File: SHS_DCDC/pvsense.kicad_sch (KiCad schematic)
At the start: 15 parts, among them Q18 BSS84, Q19 2N7002, U3 LMV324AIDR

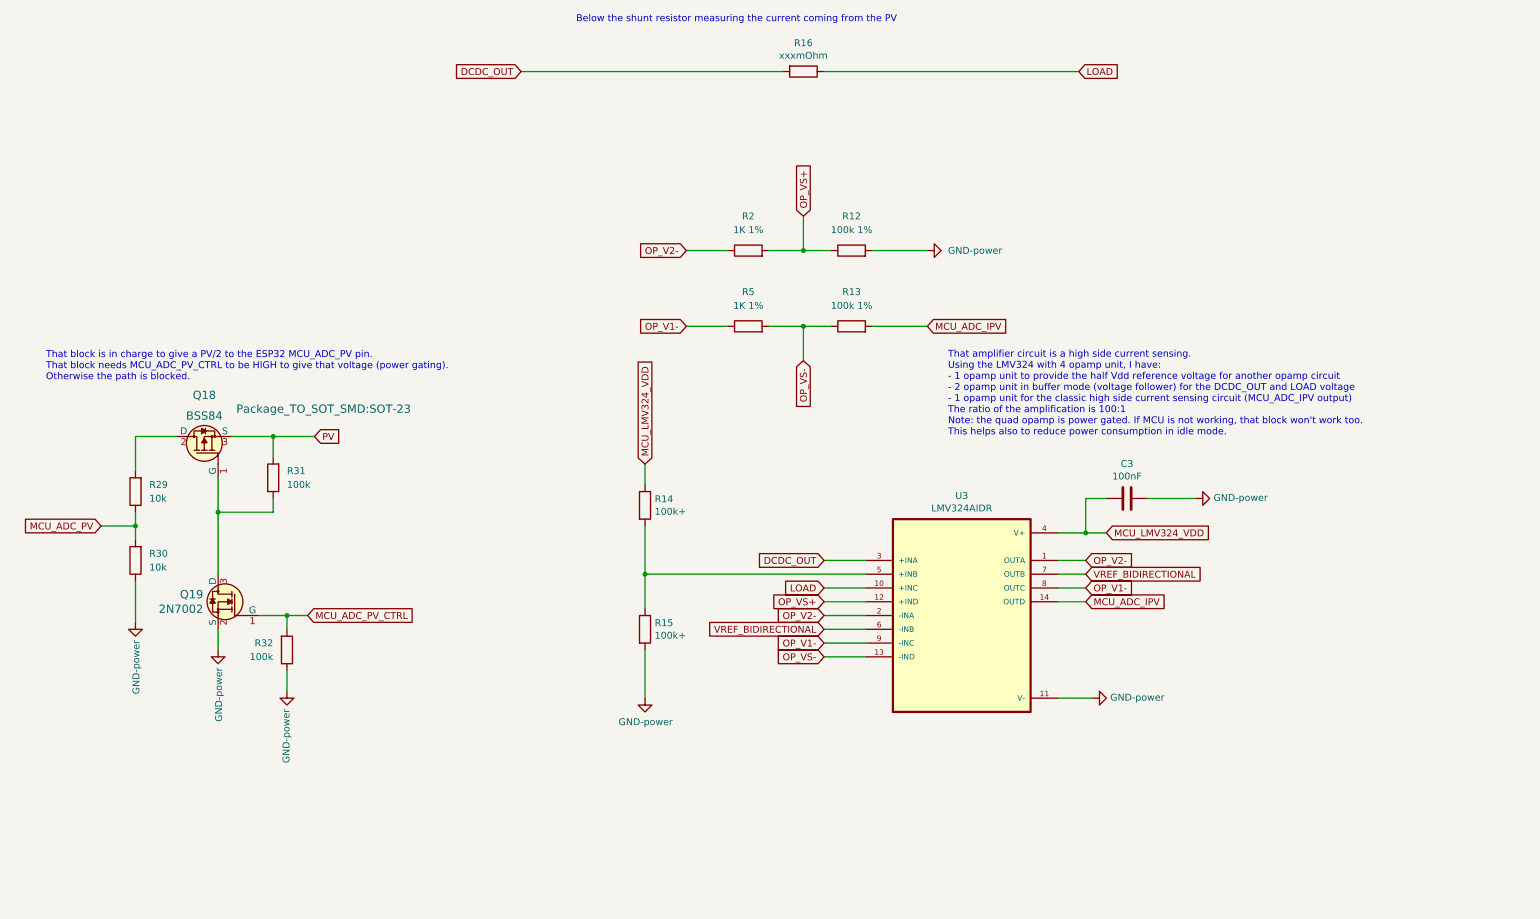
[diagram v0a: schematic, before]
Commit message: Commit before reannotation
Plan to test the reannotation feature.
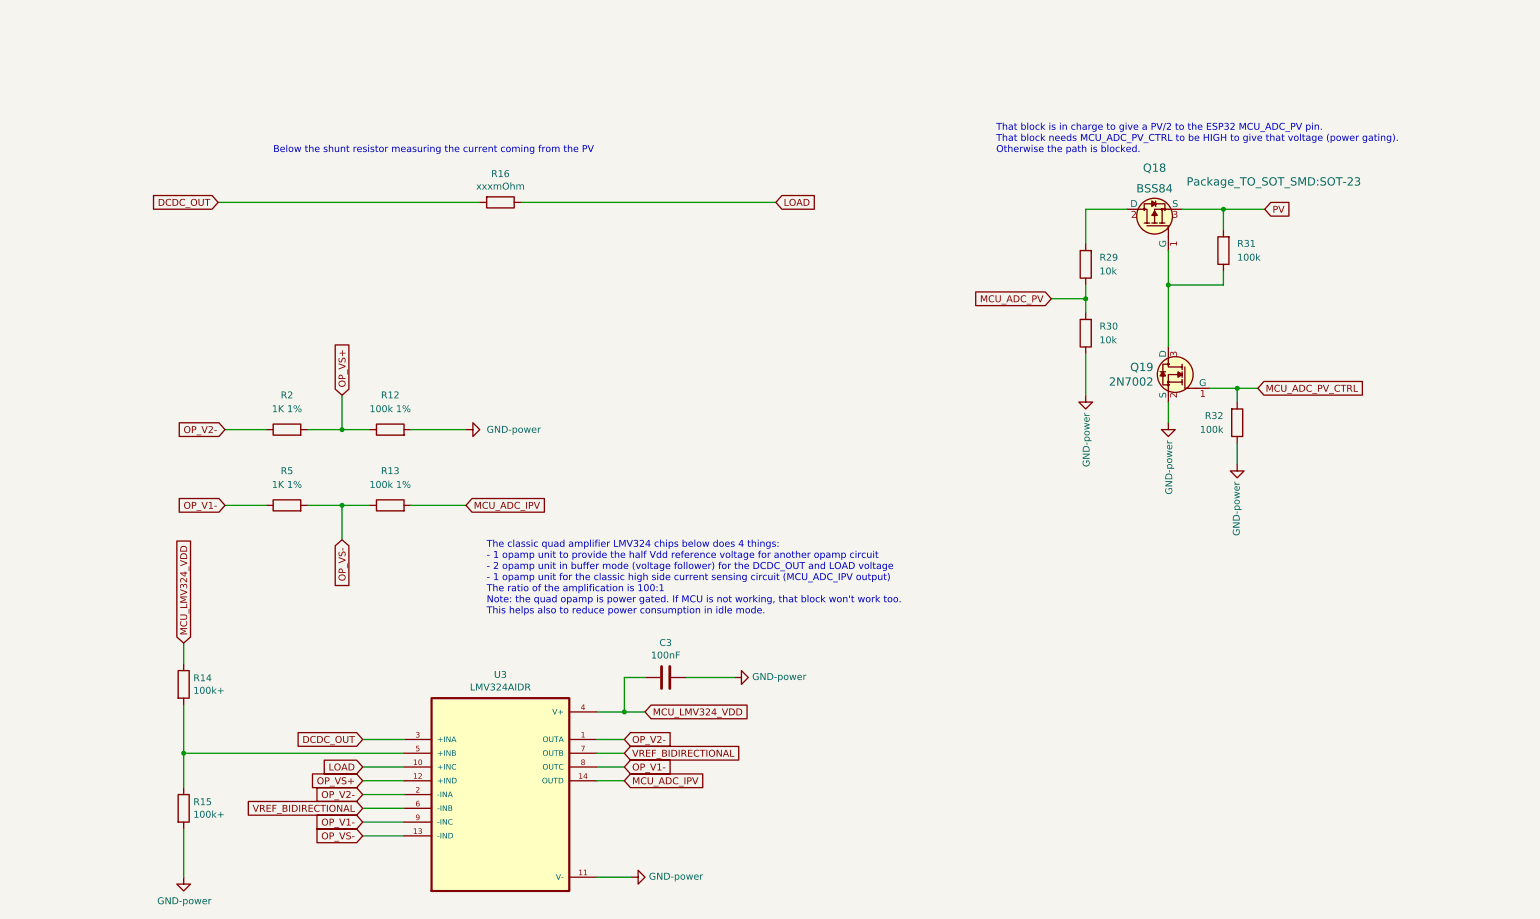
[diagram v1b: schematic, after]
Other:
- note added: "The classic quad amplifier LMV324 chips below does 4 things: - 1 opamp unit to provide the half Vdd reference voltage for another opamp circuit - 2 opamp unit in buffer mode (voltage follower) for the DCDC_OUT and LOAD voltage - 1 opamp unit for the classic high side current sensing circuit (MCU_ADC_IPV output) The ratio of the amplification is 100:1 Note: the quad opamp is power gated. If MCU is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"
- note removed: "That amplifier circuit is a high side current sensing. Using the LMV324 with 4 opamp unit, I have: - 1 opamp unit to provide the half Vdd reference voltage for another opamp circuit - 2 opamp unit in buffer mode (voltage follower) for the DCDC_OUT and LOAD voltage - 1 opamp unit for the classic high side current sensing circuit (MCU_ADC_IPV output) The ratio of the amplification is 100:1 Note: th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"
- moved on the sheet: C3, Q18, Q19, R12, R13, R14, R15, R16, R2, R29, R30, R31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

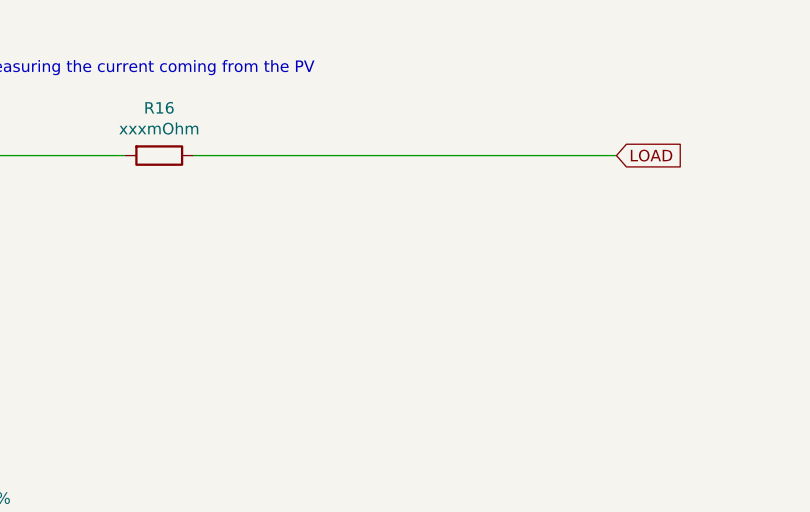
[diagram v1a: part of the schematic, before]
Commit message: Testpoints
All the tests points have been placed
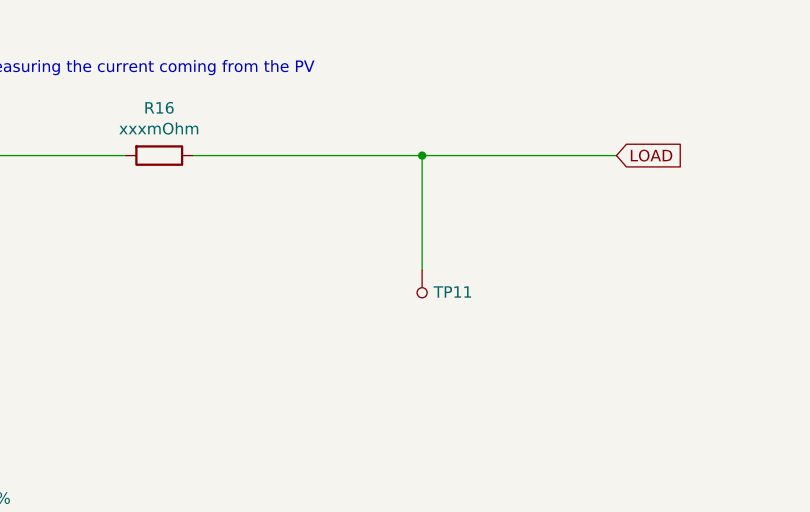
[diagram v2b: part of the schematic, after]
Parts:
- added TP11: 5029, digikey-footprints:PC_Test_Point_Mini_3.8x2.03mm, symbol dk_Test-Points:5029
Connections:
- net LOAD: now also TP11.1
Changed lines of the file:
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@@
   (junction (at 234.95 54.61) (diameter 0) (color 0 0 0 0)
   )
+  (junction (at 130.81 53.34) (diameter 0) (color 0 0 0 0)
+  )
   (junction (at 224.79 68.58) (diameter 0) (color 0 0 0 0)
   )
@@
     (stroke (width 0) (type default) (color 0 0 0 0))
   )
+  (wire (pts (xy 130.81 53.34) (xy 152.4 53.34))
+    (stroke (width 0) (type default) (color 0 0 0 0))
+  )
   (wire (pts (xy 85.09 109.22) (xy 95.25 109.22))
     (stroke (width 0) (type default) (color 0 0 0 0))
@@
     (stroke (width 0) (type default) (color 0 0 0 0))
   )
+  (wire (pts (xy 130.81 53.34) (xy 130.81 66.04))
+    (stroke (width 0) (type default) (color 0 0 0 0))
+  )
   (wire (pts (xy 43.18 138.43) (xy 43.18 134.62))
     (stroke (width 0) (type default) (color 0 0 0 0))
@@
     (stroke (width 0) (type default) (color 0 0 0 0))
   )
-  (wire (pts (xy 105.41 53.34) (xy 152.4 53.34))
+  (wire (pts (xy 105.41 53.34) (xy 130.81 53.34))
     (stroke (width 0) (type default) (color 0 0 0 0))
   )
@@
     )
     (pin "1")
+  )
+  (symbol (lib_id "dk_Test-Points:5029") (at 130.81 68.58 0) (unit 1)
+    (in_bom yes) (on_board yes) (fields_autoplaced)
+    (property "Reference" "TP11" (id 0) (at 132.08 68.5418 0)
+      (effects (font (size 1.27 1.27)) (justify left))
+    )
+    (property "Value" "5029" (id 1) (at 130.81 71.12 0)
+      (effects (font (size 1.27 1.27)) hide)
+    )
+    (property "Footprint" "digikey-footprints:PC_Test_Point_Mini_3.8x2.03mm" (id 2) (at 135.89 63.5 0)
+      (effects (font (size 1.524 1.524)) (justify left) hide)
+    )
+    (property "Datasheet" "http://www.keyelco.com/product-pdf.cfm?p=1358" (id 3) (at 135.89 60.96 0)
+      (effects (font (size 1.524 1.524)) (justify left) hide)
+    )
+    (property "Digi-Key_PN" "36-5029CT-ND" (id 4) (at 135.89 58.42 0)
+      (effects (font (size 1.524 1.524)) (justify left) hide)
+    )
+    (property "MPN" "5029" (id 5) (at 135.89 55.88 0)
+      (effects (font (size 1.524 1.524)) (justify left) hide)
+    )
+    (property "Category" "Test and Measurement" (id 6) (at 135.89 53.34 0)
+      (effects (font (size 1.524 1.524)) (justify left) hide)
+    )
+    (property "Family" "Test Points" (id 7) (at 135.89 50.8 0)
+      (effects (font (size 1.524 1.524)) (justify left) hide)
+    )
+    (property "DK_Datasheet_Link" "http://www.keyelco.com/product-pdf.cfm?p=1358" (id 8) (at 135.89 48.26 0)
+      (effects (font (size 1.524 1.524)) (justify left) hide)
+    )
+    (property "DK_Detail_Page" "/product-detail/en/keystone-electronics/5029/36-5029CT-ND/5980631" (id 9) (at 135.89 45.72 0)
+      (effects (font (size 1.524 1.524)) (justify left) hide)
+    )
+    (property "Description" "PC TEST POINT MINIATURE" (id 10) (at 135.89 43.18 0)
+      (effects (font (size 1.524 1.524)) (justify left) hide)
+    )
+    (property "Manufacturer" "Keystone Electronics" (id 11) (at 135.89 40.64 0)
+      (effects (font (size 1.524 1.524)) (justify left) hide)
+    )
+    (property "Status" "Active" (id 12) (at 135.89 38.1 0)
+      (effects (font (size 1.524 1.524)) (justify left) hide)
+    )
+    (pin "1")
